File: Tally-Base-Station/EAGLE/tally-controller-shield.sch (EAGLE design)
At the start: 24 parts, among them J2 Mega R3, U1 SN75174N, U2 SN75174N, U3 SN75174N

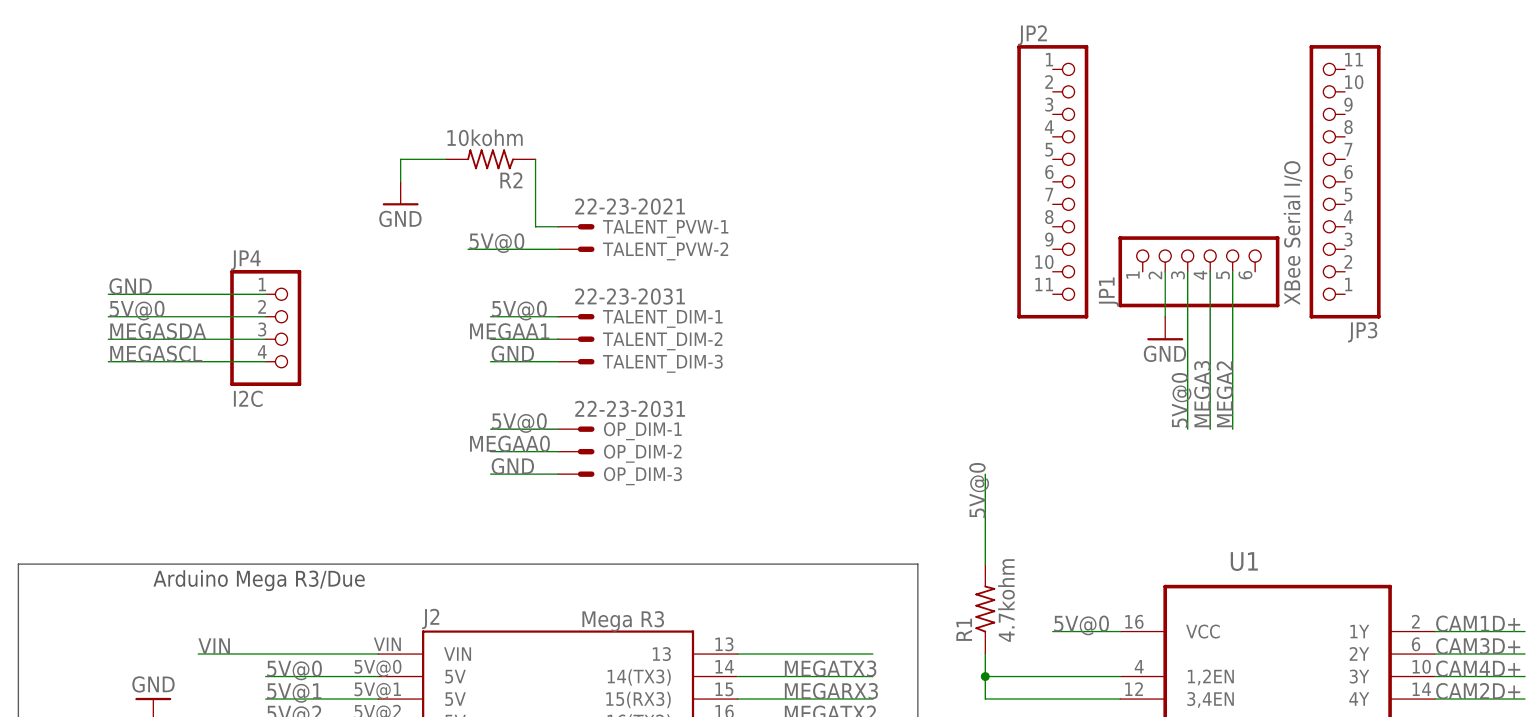
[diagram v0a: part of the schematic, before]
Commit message: Add some additional headers, fix switch wiring.
Add extra I2C connector that will work with a right-angle header.
Add a neopixel header for a possible system status light.
Wire switch to input (missed that in the schematic)
Trim the number of headers for holding the XBee regulated breakout to make routing easier
Add a bunch of labels to things on the top silkscreen.
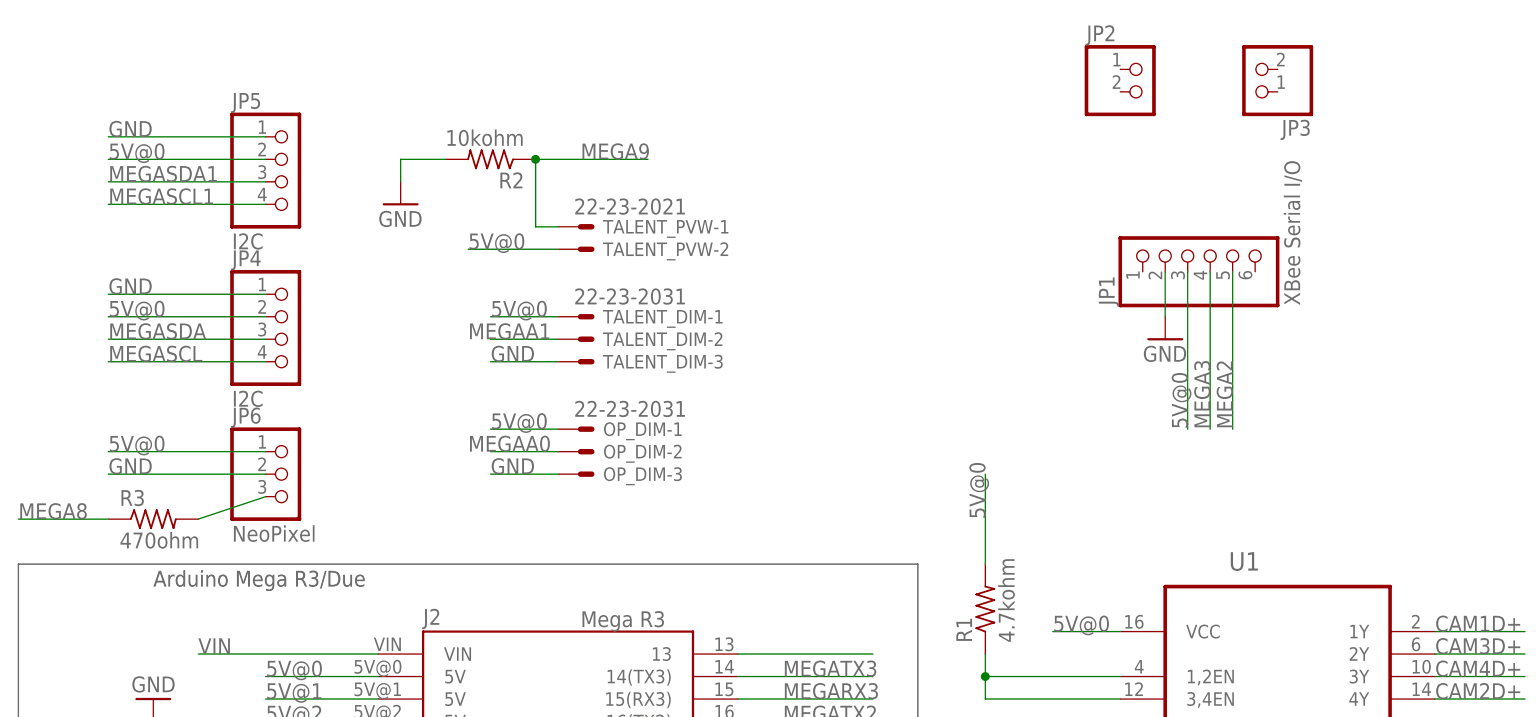
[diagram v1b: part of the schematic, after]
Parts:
- added JP5: I2C, pinhead:PINHD-1X4
- added JP6: NeoPixel, pinhead:PINHD-1X3
- added R3: 470ohm, rcl:R-US_0207/10
- JP2, JP3: device pinhead:PINHD-1X11 -> pinhead:PINHD-1X2
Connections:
- removed net N$1: R2.1, TALENT_PVW-1.S
- new net NEOPIXELDATA: JP6.3, R3.2
- net 5V@0: now also JP5.2, JP6.1
- net GND: now also JP5.1, JP6.2
- net MEGA8: now also R3.1
- net MEGA9: now also R2.1, TALENT_PVW-1.S
- net MEGASCL1: now also JP5.4
- net MEGASDA1: now also JP5.3
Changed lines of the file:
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@@
 <parts>
 <part name="J2" library="zortness" deviceset="ARDUINO-MEGA" device="FULL" value="Mega R3"/>
-<part name="GND" library="supply1" deviceset="GND" device=""/>
-<part name="GND37" library="supply1" deviceset="GND" device=""/>
+<part name="GND" library="supply1" library_urn="urn:adsk.eagle:library:371" deviceset="GND" device=""/>
+<part name="GND37" library="supply1" library_urn="urn:adsk.eagle:library:371" deviceset="GND" device=""/>
 <part name="S1" library="zortness" deviceset="TAC_SWITCH" device="KMR2" value="KMR2"/>
 <part name="CAM1" library="con-molex" library_urn="urn:adsk.eagle:library:165" deviceset="22-23-2021" device="" package3d_urn="urn:adsk.eagle:package:8078633/1"/>
@@
 <part name="GND3" library="supply1" library_urn="urn:adsk.eagle:library:371" deviceset="GND" device=""/>
 <part name="JP1" library="pinhead" library_urn="urn:adsk.eagle:library:325" deviceset="PINHD-1X6" device="" package3d_urn="urn:adsk.eagle:package:22472/2" value="XBee Serial I/O"/>
-<part name="JP2" library="pinhead" library_urn="urn:adsk.eagle:library:325" deviceset="PINHD-1X11" device="" package3d_urn="urn:adsk.eagle:package:22410/2"/>
-<part name="JP3" library="pinhead" library_urn="urn:adsk.eagle:library:325" deviceset="PINHD-1X11" device="" package3d_urn="urn:adsk.eagle:package:22410/2"/>
 <part name="GND4" library="supply1" library_urn="urn:adsk.eagle:library:371" deviceset="GND" device=""/>
 <part name="TALENT_PVW" library="con-molex" library_urn="urn:adsk.eagle:library:165" deviceset="22-23-2021" device="" package3d_urn="urn:adsk.eagle:package:8078633/1"/>
@@
 <part name="GND5" library="supply1" library_urn="urn:adsk.eagle:library:371" deviceset="GND" device=""/>
 <part name="JP4" library="pinhead" library_urn="urn:adsk.eagle:library:325" deviceset="PINHD-1X4" device="" package3d_urn="urn:adsk.eagle:package:22407/2" value="I2C"/>
+<part name="JP5" library="pinhead" library_urn="urn:adsk.eagle:library:325" deviceset="PINHD-1X4" device="" package3d_urn="urn:adsk.eagle:package:22407/2" value="I2C"/>
+<part name="JP6" library="pinhead" library_urn="urn:adsk.eagle:library:325" deviceset="PINHD-1X3" device="" package3d_urn="urn:adsk.eagle:package:22458/2" value="NeoPixel"/>
+<part name="R3" library="rcl" library_urn="urn:adsk.eagle:library:334" deviceset="R-US_" device="0207/10" package3d_urn="urn:adsk.eagle:package:23491/2" value="470ohm"/>
+<part name="JP2" library="pinhead" library_urn="urn:adsk.eagle:library:325" deviceset="PINHD-1X2" device="" package3d_urn="urn:adsk.eagle:package:22435/2"/>
+<part name="JP3" library="pinhead" library_urn="urn:adsk.eagle:library:325" deviceset="PINHD-1X2" device="" package3d_urn="urn:adsk.eagle:package:22435/2"/>
 </parts>
 <sheets>
@@
 <attribute name="VALUE" x="-15.24" y="140.97" size="1.778" layer="96" rot="R90"/>
 </instance>
-<instance part="JP2" gate="A" x="-40.64" y="154.94" smashed="yes">
-<attribute name="NAME" x="-46.99" y="170.815" size="1.778" layer="95"/>
-<attribute name="VALUE" x="-46.99" y="137.16" size="1.778" layer="96"/>
-</instance>
-<instance part="JP3" gate="A" x="-12.7" y="154.94" smashed="yes" rot="R180">
-<attribute name="NAME" x="-6.35" y="139.065" size="1.778" layer="95" rot="R180"/>
-<attribute name="VALUE" x="-6.35" y="172.72" size="1.778" layer="96" rot="R180"/>
-</instance>
 <instance part="GND4" gate="1" x="-30.48" y="137.16" smashed="yes">
 <attribute name="VALUE" x="-33.02" y="134.62" size="1.778" layer="96"/>
@@
 <attribute name="NAME" x="-135.89" y="145.415" size="1.778" layer="95"/>
 <attribute name="VALUE" x="-135.89" y="129.54" size="1.778" layer="96"/>
+</instance>
+<instance part="JP5" gate="A" x="-129.54" y="154.94" smashed="yes">
+<attribute name="NAME" x="-135.89" y="163.195" size="1.778" layer="95"/>
+<attribute name="VALUE" x="-135.89" y="147.32" size="1.778" layer="96"/>
+</instance>
+<instance part="JP6" gate="A" x="-129.54" y="121.92" smashed="yes">
+<attribute name="NAME" x="-135.89" y="127.635" size="1.778" layer="95"/>
+<attribute name="VALUE" x="-135.89" y="114.3" size="1.778" layer="96"/>
+</instance>
+<instance part="R3" gate="G$1" x="-144.78" y="116.84" smashed="yes">
+<attribute name="NAME" x="-148.59" y="118.3386" size="1.778" layer="95"/>
+<attribute name="VALUE" x="-148.59" y="113.538" size="1.778" layer="96"/>
+</instance>
+<instance part="JP2" gate="G$1" x="-33.02" y="165.1" smashed="yes">
+<attribute name="NAME" x="-39.37" y="170.815" size="1.778" layer="95"/>
+<attribute name="VALUE" x="-39.37" y="160.02" size="1.778" layer="96"/>
+</instance>
+<instance part="JP3" gate="G$1" x="-20.32" y="167.64" smashed="yes" rot="R180">
+<attribute name="NAME" x="-13.97" y="161.925" size="1.778" layer="95" rot="R180"/>
+<attribute name="VALUE" x="-13.97" y="172.72" size="1.778" layer="96" rot="R180"/>
 </instance>
 </instances>
@@
 <wire x1="-116.84" y1="157.48" x2="-116.84" y2="154.94" width="0.1524" layer="91"/>
 </segment>
+<segment>
+<pinref part="JP5" gate="A" pin="1"/>
+<wire x1="-132.08" y1="160.02" x2="-149.86" y2="160.02" width="0.1524" layer="91"/>
+<label x="-149.86" y="160.02" size="1.778" layer="95"/>
+</segment>
+<segment>
+<pinref part="JP6" gate="A" pin="2"/>
+<wire x1="-132.08" y1="121.92" x2="-149.86" y2="121.92" width="0.1524" layer="91"/>
+<label x="-149.86" y="121.92" size="1.778" layer="95"/>
+</segment>
 </net>
 <net name="MEGASDA" class="0">
@@
 <wire x1="-119.38" y1="20.32" x2="-139.7" y2="20.32" width="0.1524" layer="91"/>
 </segment>
+<segment>
+<pinref part="R3" gate="G$1" pin="1"/>
+<wire x1="-149.86" y1="116.84" x2="-160.02" y2="116.84" width="0.1524" layer="91"/>
+<label x="-160.02" y="116.84" size="1.778" layer="95"/>
+</segment>
 </net>
 <net name="MEGA7" class="0">
@@
 <wire x1="-119.38" y1="17.78" x2="-139.7" y2="17.78" width="0.1524" layer="91"/>
 </segment>
+<segment>
+<wire x1="-88.9" y1="157.48" x2="-101.6" y2="157.48" width="0.1524" layer="91"/>
+<pinref part="TALENT_PVW" gate="-1" pin="S"/>
+<wire x1="-99.06" y1="149.86" x2="-101.6" y2="149.86" width="0.1524" layer="91"/>
+<pinref part="R2" gate="G$1" pin="1"/>
+<wire x1="-101.6" y1="149.86" x2="-101.6" y2="157.48" width="0.1524" layer="91"/>
+<junction x="-101.6" y="157.48"/>
+<label x="-96.52" y="157.48" size="1.778" layer="95"/>
+</segment>
 </net>
 <net name="MEGA10" class="0">
@@
 <label x="-76.2" y="-5.08" size="1.778" layer="95"/>
 </segment>
+<segment>
+<pinref part="JP5" gate="A" pin="3"/>
+<wire x1="-132.08" y1="154.94" x2="-149.86" y2="154.94" width="0.1524" layer="91"/>
+<label x="-149.86" y="154.94" size="1.778" layer="95"/>
+</segment>
 </net>
 <net name="MEGASCL1" class="0">
@@
 <wire x1="-78.74" y1="-2.54" x2="-63.5" y2="-2.54" width="0.1524" layer="91"/>
 <label x="-76.2" y="-2.54" size="1.778" layer="95"/>
+</segment>
+<segment>
+<pinref part="JP5" gate="A" pin="4"/>
+<wire x1="-132.08" y1="152.4" x2="-149.86" y2="152.4" width="0.1524" layer="91"/>
+<label x="-149.86" y="152.4" size="1.778" layer="95"/>
 </segment>
 </net>
@@
 <label x="-50.8" y="116.84" size="1.778" layer="95" rot="R90"/>
 </segment>
+<segment>
+<pinref part="JP5" gate="A" pin="2"/>
+<wire x1="-132.08" y1="157.48" x2="-149.86" y2="157.48" width="0.1524" layer="91"/>
+<label x="-149.86" y="157.48" size="1.778" layer="95"/>
+</segment>
+<segment>
+<pinref part="JP6" gate="A" pin="1"/>
+<wire x1="-132.08" y1="124.46" x2="-149.86" y2="124.46" width="0.1524" layer="91"/>
+<label x="-149.86" y="124.46" size="1.778" layer="95"/>
+</segment>
 </net>
 <net name="5V@1" class="0">
@@
 </segment>
 </net>
-<net name="N$1" class="0">
-<segment>
-<pinref part="TALENT_PVW" gate="-1" pin="S"/>
-<wire x1="-99.06" y1="149.86" x2="-101.6" y2="149.86" width="0.1524" layer="91"/>
-<pinref part="R2" gate="G$1" pin="1"/>
-<wire x1="-101.6" y1="149.86" x2="-101.6" y2="157.48" width="0.1524" layer="91"/>
-</segment>
-</net>
+<net name="NEOPIXELDATA" class="0">
+<segment>
+<pinref part="JP6" gate="A" pin="3"/>
+<wire x1="-132.08" y1="119.38" x2="-139.7" y2="116.84" width="0.1524" layer="91"/>
+<pinref part="R3" gate="G$1" pin="2"/>
+</segment>
+</net>

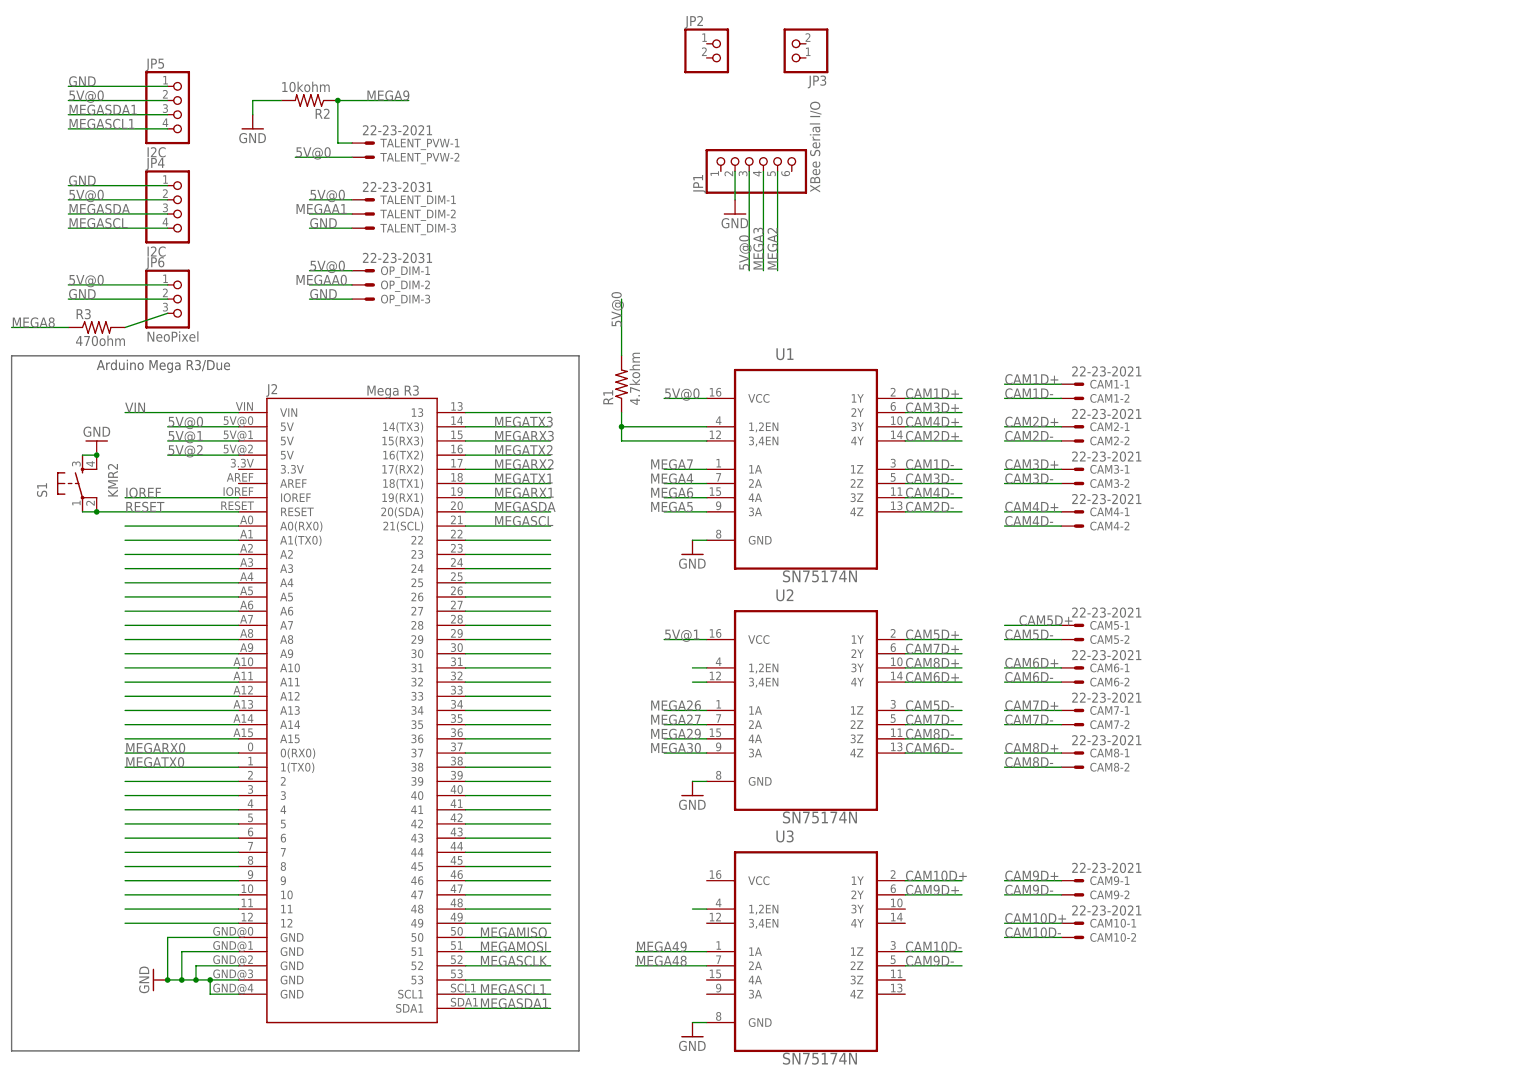
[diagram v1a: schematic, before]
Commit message: Major rework of the shield to make a much better layout.
- Expanded to 12 camera support out of the box
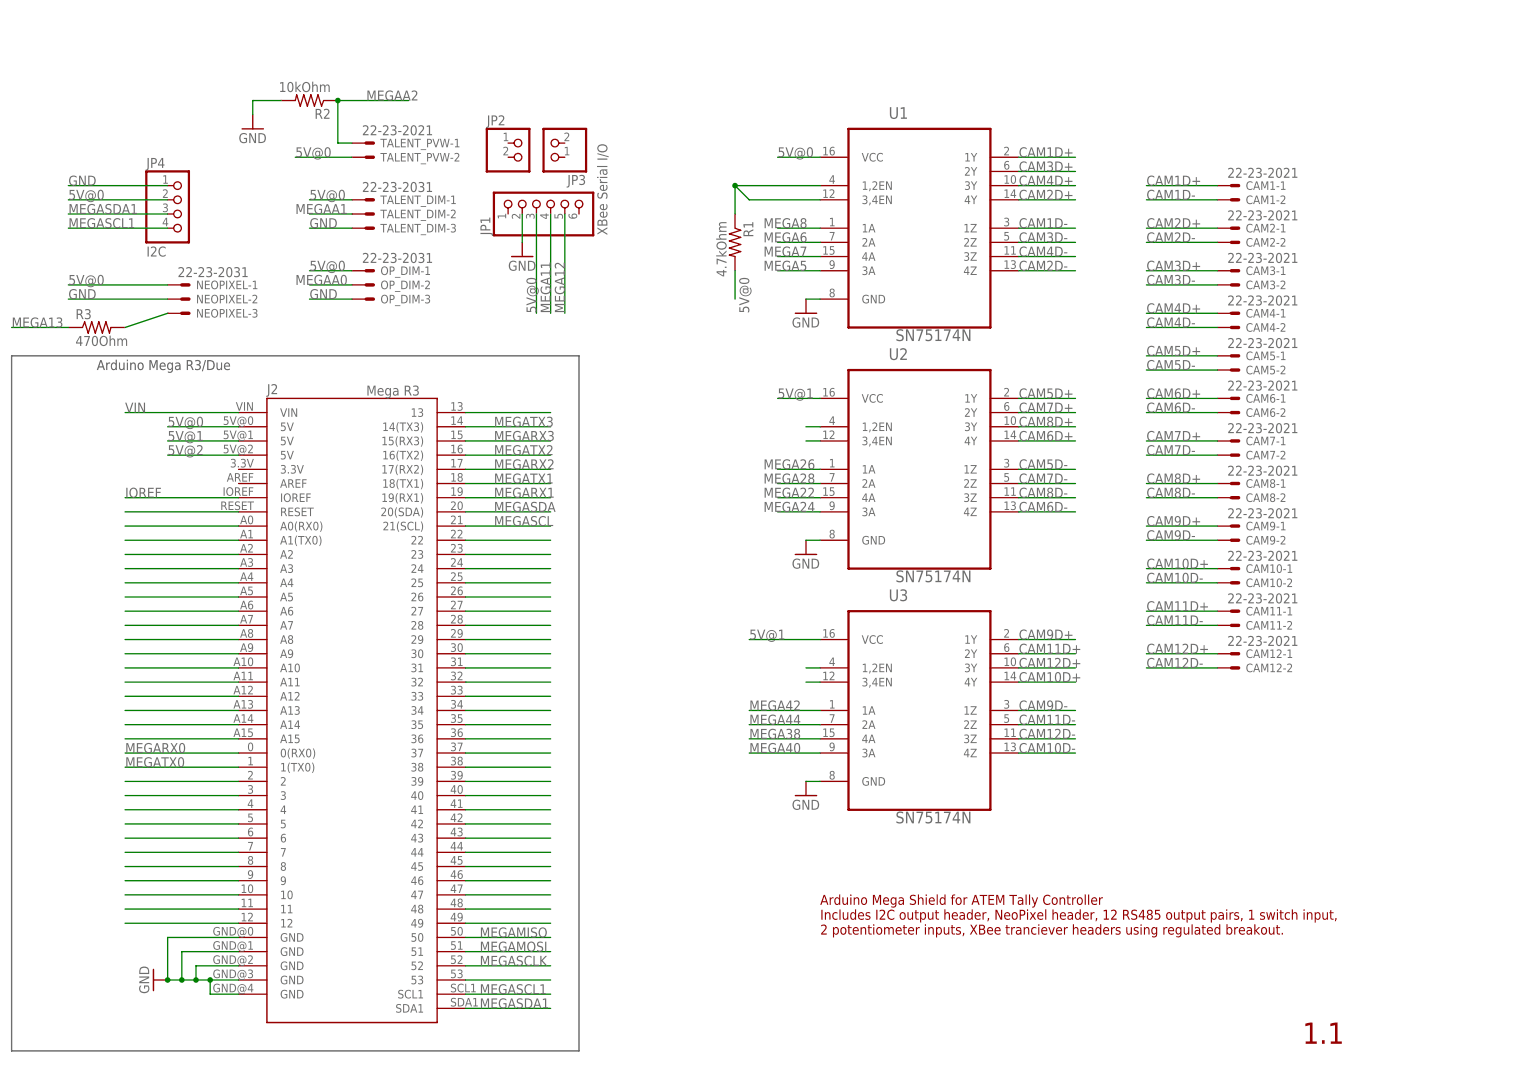
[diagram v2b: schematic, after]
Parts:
- removed JP5: I2C, pinhead:PINHD-1X4
- removed JP6: NeoPixel, pinhead:PINHD-1X3
- removed S1: KMR2, zortness:TAC_SWITCHKMR2
- added CAM11, CAM12: 22-23-2021, con-molex:22-23-2021
- added NEOPIXEL: 22-23-2031, con-molex:22-23-2031
- R1: value 4.7kohm -> 4.7kOhm
- R2: value 10kohm -> 10kOhm
- R3: value 470ohm -> 470Ohm
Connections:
- new net CAM11D+: CAM11-1.S, U3.2Y
- new net CAM11D-: CAM11-2.S, U3.2Z
- new net CAM12D+: CAM12-1.S, U3.3Y
- new net CAM12D-: CAM12-2.S, U3.3Z
- net 5V@0: now also NEOPIXEL-1.S; no longer JP5.2, JP6.1
- net 5V@1: now also U3.VCC
- net CAM10D+: now also U3.4Y; no longer U3.1Y
- net CAM10D-: now also U3.4Z; no longer U3.1Z
- net CAM9D+: now also U3.1Y; no longer U3.2Y
- net CAM9D-: now also U3.1Z; no longer U3.2Z
- net GND: now also NEOPIXEL-2.S; no longer JP5.1, JP6.2, S1.3, S1.4
- net MEGA11: now also JP1.4
- net MEGA12: now also JP1.5
- net MEGA13: now also R3.1
- net MEGA2: no longer JP1.5
- net MEGA22: now also U2.4A
- net MEGA24: now also U2.3A
- net MEGA27: no longer U2.2A
- net MEGA28: now also U2.2A
- net MEGA29: no longer U2.4A
- net MEGA3: no longer JP1.4
- net MEGA30: no longer U2.3A
- net MEGA38: now also U3.4A
- net MEGA4: no longer U1.2A
- net MEGA40: now also U3.3A
- net MEGA42: now also U3.1A
- net MEGA44: now also U3.2A
- net MEGA48: no longer U3.2A
- net MEGA49: no longer U3.1A
- net MEGA6: now also U1.2A; no longer U1.4A
- net MEGA7: now also U1.4A; no longer U1.1A
- net MEGA8: now also U1.1A; no longer R3.1
- net MEGA9: no longer R2.1, TALENT_PVW-1.S
- net MEGAA2: now also R2.1, TALENT_PVW-1.S
- net MEGASCL: no longer JP4.4
- net MEGASCL1: now also JP4.4; no longer JP5.4
- net MEGASDA: no longer JP4.3
- net MEGASDA1: now also JP4.3; no longer JP5.3
- net NEOPIXELDATA: now also NEOPIXEL-3.S; no longer JP6.3
- net RESET: no longer S1.1, S1.2
- net RS485EN: now also U3.3,4EN
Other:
- note added: "1.1"
- note added: "Arduino Mega Shield for ATEM Tally Controller Includes I2C output header, NeoPixel header, 12 RS485 output pairs, 1 switch input, 2 potentiometer inputs, XBee tranciever headers using regulated breakout."
- moved on the sheet: CAM1-1, CAM1-2, CAM10-1, CAM10-2, CAM2-1, CAM2-2, CAM3-1, CAM3-2, CAM4-1, CAM4-2, CAM5-1, CAM5-2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
